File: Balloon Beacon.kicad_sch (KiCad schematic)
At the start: 51 parts, among them J1 PV Input, J2 Serial, J3 ICSP, J4 I2C, J6 GPS_ANT, Q1 AO3401A, U1 CJ431, U2 ATmega328PB-MU, U3 STC22K33048-26.000MT, U4 LM50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

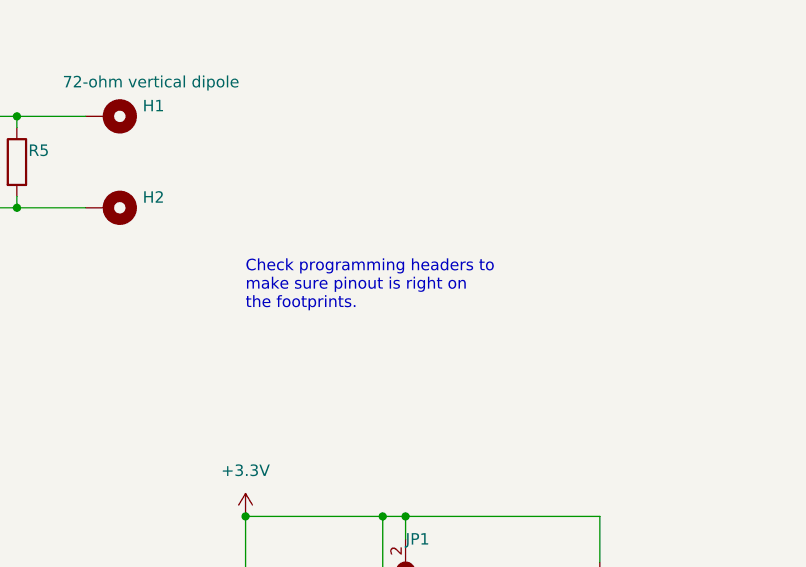
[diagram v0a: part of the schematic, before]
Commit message: Deleted note on schematic and added footprint for jumper.
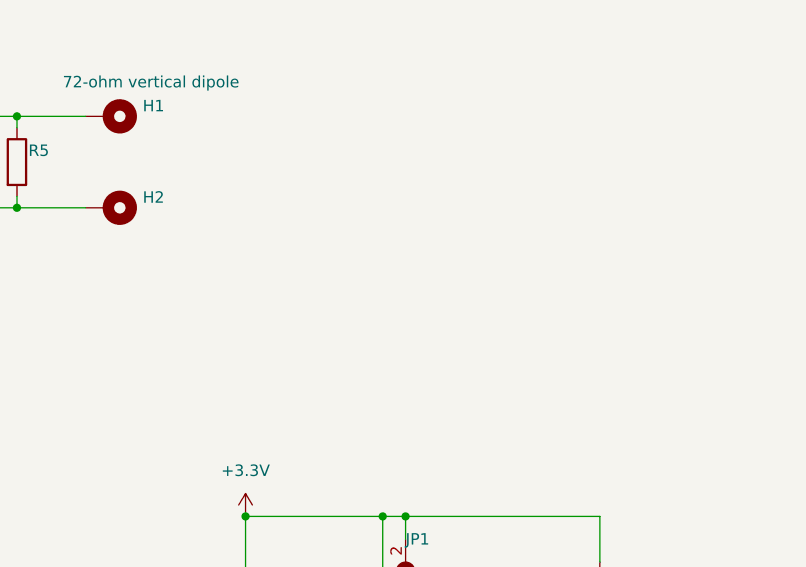
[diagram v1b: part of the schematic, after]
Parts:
- JP1: footprint (none) -> Jumper:SolderJumper-2_P1.3mm_Open_TrianglePad1.0x1.5mm
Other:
- note removed: "Check programming headers to make sure pinout is right on the footprints."
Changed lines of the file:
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@@
-    (effects (font (size 1.27 1.27)) (justify left bottom))
-  )
-  (text "Check programming headers to \nmake sure pinout is right on\nthe footprints."
-    (at 205.74 58.42 0)
     (effects (font (size 1.27 1.27)) (justify left bottom))
   )
@@
       (effects (font (size 1.27 1.27)) (justify right) hide)
     )
-    (property "Footprint" "" (id 2) (at 223.52 87.63 0)
+    (property "Footprint" "Jumper:SolderJumper-2_P1.3mm_Open_TrianglePad1.0x1.5mm" (id 2) (at 223.52 87.63 0)
       (effects (font (size 1.27 1.27)) hide)
     )
@@
     )
     (path "/7acad855-ca17-4ab1-8fa0-6bf876855ebd"
-      (reference "JP1") (unit 1) (value "SolderJumper_2_Open") (footprint "")
+      (reference "JP1") (unit 1) (value "SolderJumper_2_Open") (footprint "Jumper:SolderJumper-2_P1.3mm_Open_TrianglePad1.0x1.5mm")
     )
     (path "/38660ac3-4961-47b0-bbb6-8ac190a31e1a"

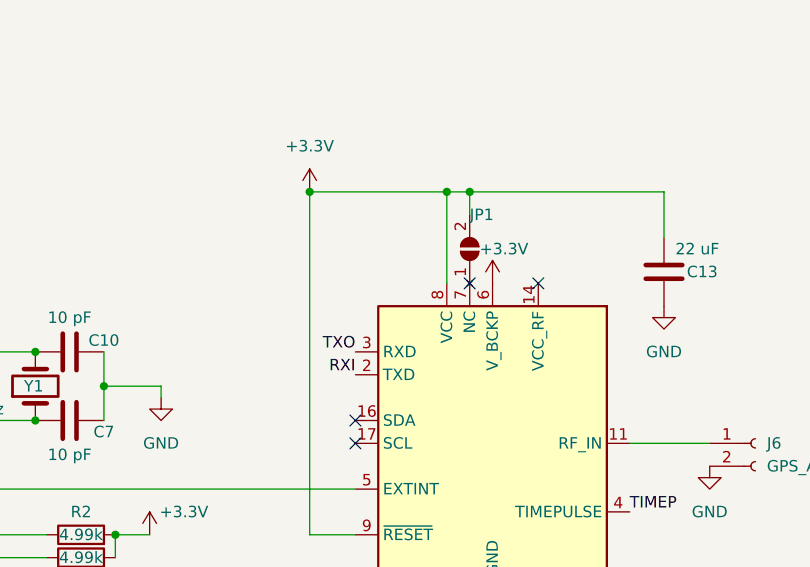
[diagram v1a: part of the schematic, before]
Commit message: Fixed no connect on GPS...
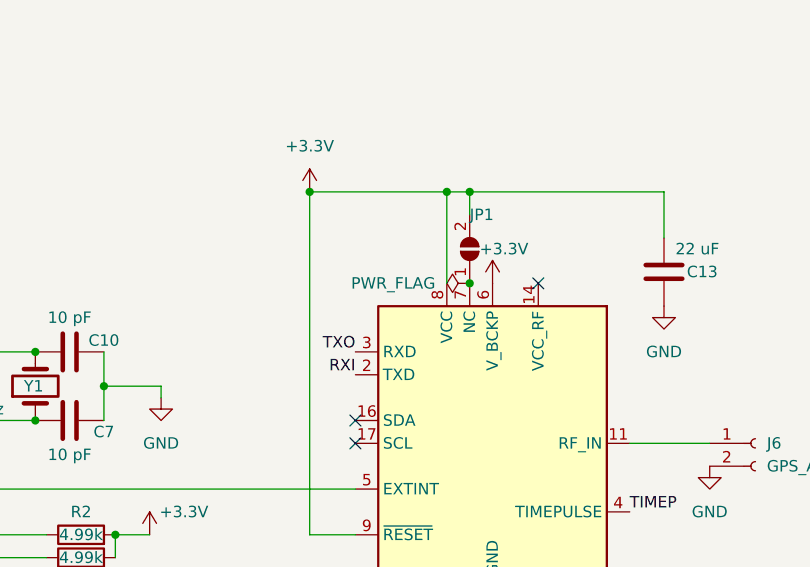
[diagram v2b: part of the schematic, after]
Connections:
- no-connect marks 15 -> 14
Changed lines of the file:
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@@
   (junction (at 205.74 81.28) (diameter 0) (color 0 0 0 0)
+  )
+  (junction (at 223.52 91.44) (diameter 0) (color 0 0 0 0)
   )
   (junction (at 182.88 102.87) (diameter 0) (color 0 0 0 0)
@@
   (no_connect (at 81.28 41.91))
   (no_connect (at 55.88 39.37))
-  (no_connect (at 223.52 91.44))
   (no_connect (at 170.18 41.91))
   (no_connect (at 20.32 34.29))
@@
     (pin "1")
   )
+  (symbol (lib_id "power:PWR_FLAG") (at 223.52 91.44 90) (unit 1)
+    (in_bom yes) (on_board yes) (fields_autoplaced)
+    (property "Reference" "#FLG?" (id 0) (at 221.615 91.44 0)
+      (effects (font (size 1.27 1.27)) hide)
+    )
+    (property "Value" "PWR_FLAG" (id 1) (at 219.71 91.4399 90)
+      (effects (font (size 1.27 1.27)) (justify left))
+    )
+    (property "Footprint" "" (id 2) (at 223.52 91.44 0)
+      (effects (font (size 1.27 1.27)) hide)
+    )
+    (property "Datasheet" "~" (id 3) (at 223.52 91.44 0)
+      (effects (font (size 1.27 1.27)) hide)
+    )
+    (pin "1")
+  )
   (symbol (lib_id "Connector:Conn_01x02_Female") (at 255.27 109.22 0) (unit 1)
     (in_bom yes) (on_board yes) (fields_autoplaced)
@@
       (reference "#FLG0104") (unit 1) (value "PWR_FLAG") (footprint "")
     )
+    (path "/e752b3c5-19d9-412d-8084-a1d633460973"
+      (reference "#FLG?") (unit 1) (value "PWR_FLAG") (footprint "")
+    )
     (path "/39681a7e-93cb-47f8-bfb9-0aecbadbf696"

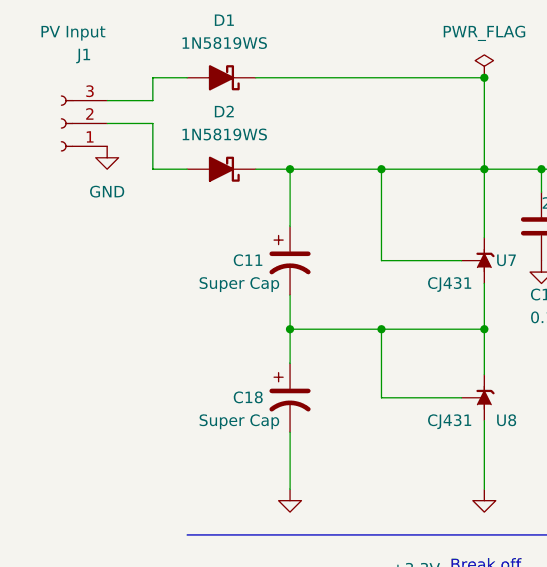
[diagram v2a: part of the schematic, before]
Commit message: Added a solar cell so you can see what might work...
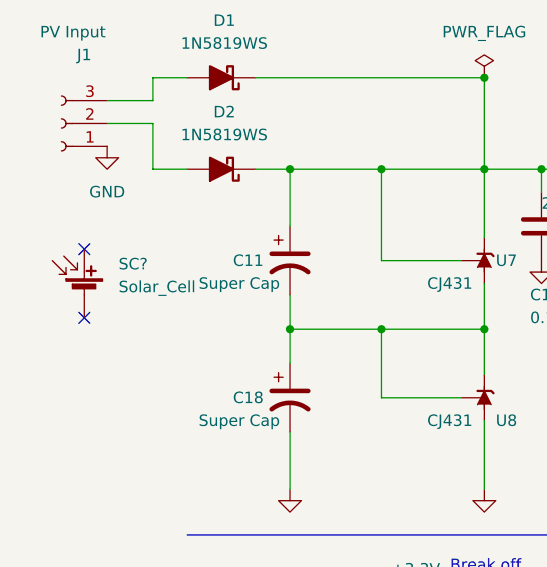
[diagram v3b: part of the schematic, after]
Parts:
- added SC?: Solar_Cell, symbol Device:Solar_Cell
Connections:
- no-connect marks 14 -> 16
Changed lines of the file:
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@@
   (no_connect (at 210.82 106.68))
   (no_connect (at 210.82 109.22))
+  (no_connect (at 20.32 118.11))
+  (no_connect (at 20.32 125.73))
   (no_connect (at 156.21 86.36))
   (no_connect (at 156.21 88.9))
@@
     (pin "1")
   )
+  (symbol (lib_id "Device:Solar_Cell") (at 20.32 123.19 0) (unit 1)
+    (in_bom yes) (on_board yes) (fields_autoplaced)
+    (property "Reference" "SC?" (id 0) (at 24.13 119.7609 0)
+      (effects (font (size 1.27 1.27)) (justify left))
+    )
+    (property "Value" "Solar_Cell" (id 1) (at 24.13 122.3009 0)
+      (effects (font (size 1.27 1.27)) (justify left))
+    )
+    (property "Footprint" "" (id 2) (at 20.32 121.666 90)
+      (effects (font (size 1.27 1.27)) hide)
+    )
+    (property "Datasheet" "https://www.mouser.com/ProductDetail/PowerFilm/MPT36-75?qs=BJlw7L4Cy79PADpX3LN7rA%3D%3D" (id 3) (at 20.32 121.666 90)
+      (effects (font (size 1.27 1.27)) hide)
+    )
+    (pin "1")
+    (pin "2")
+  )
   (symbol (lib_id "Device:C") (at 45.72 34.29 270) (unit 1)
     (in_bom yes) (on_board yes)
@@
   (symbol (lib_id "power:PWR_FLAG") (at 223.52 91.44 90) (unit 1)
     (in_bom yes) (on_board yes) (fields_autoplaced)
-    (property "Reference" "#FLG?" (id 0) (at 221.615 91.44 0)
+    (property "Reference" "#FLG0103" (id 0) (at 221.615 91.44 0)
       (effects (font (size 1.27 1.27)) hide)
     )
@@
       (reference "#FLG0102") (unit 1) (value "PWR_FLAG") (footprint "")
     )
+    (path "/e752b3c5-19d9-412d-8084-a1d633460973"
+      (reference "#FLG0103") (unit 1) (value "PWR_FLAG") (footprint "")
+    )
     (path "/578ae771-eb1e-452e-ad8f-2873091bd97f"
       (reference "#FLG0104") (unit 1) (value "PWR_FLAG") (footprint "")
     )
-    (path "/e752b3c5-19d9-412d-8084-a1d633460973"
-      (reference "#FLG?") (unit 1) (value "PWR_FLAG") (footprint "")
-    )
     (path "/39681a7e-93cb-47f8-bfb9-0aecbadbf696"
       (reference "#PWR01") (unit 1) (value "GND") (footprint "")
@@
       (reference "R8") (unit 1) (value "100") (footprint "Resistor_SMD:R_0603_1608Metric_Pad0.98x0.95mm_HandSolder")
     )
+    (path "/636dce35-ff98-43a1-aeb4-4c95a15832a9"
+      (reference "SC?") (unit 1) (value "Solar_Cell") (footprint "")
+    )
     (path "/02163717-eac1-4757-bdb2-c94f527ed6dd"

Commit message: Changed JLCPCB to LCSC for compatibility with https://support.jlcpcb.com/article/84-how-to-generate-the-bom-and-centroid-file-from-kicad
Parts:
- C10, C7: JLCPCB C1634 -> (none); LCSC (none) -> C1634
- C12, C14, C15, C16, C17, C19, C5, C6, C8, C9: JLCPCB C1525 -> (none); LCSC (none) -> C1525
- C13, C3: JLCPCB C59461 -> (none); LCSC (none) -> C59461
- C2: JLCPCB C1620 -> (none); LCSC (none) -> C1620
- C4: JLCPCB C51207 -> (none); LCSC (none) -> C51207
- D1, D2: JLCPCB C191023 -> (none); LCSC (none) -> C191023
- D4: JLCPCB C2293 -> (none); LCSC (none) -> C2293
- Q1: JLCPCB C15127 -> (none); LCSC (none) -> C15127
- R1, R5: JLCPCB C17490 -> (none); LCSC (none) -> C17490
- R2, R3: JLCPCB C23046 -> (none); LCSC (none) -> C23046
- R4: JLCPCB C22843 -> (none); LCSC (none) -> C22843
- R6: JLCPCB C23172 -> (none); LCSC (none) -> C23172
- R7: JLCPCB C25741 -> (none); LCSC (none) -> C25741
- R8: JLCPCB C22775 -> (none); LCSC (none) -> C22775
- U1, U7, U8: JLCPCB C3113 -> (none); LCSC (none) -> C3113
- U2: JLCPCB C967933 -> (none); LCSC (none) -> C967933
- U4: JLCPCB C411880 -> (none); LCSC (none) -> C411880
- U5: JLCPCB C504891 -> (none); LCSC (none) -> C504891
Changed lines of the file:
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@@
       (effects (font (size 1.27 1.27) italic) hide)
     )
-    (property "JLCPCB" "C3113" (id 4) (at 102.87 119.38 90)
+    (property "LCSC" "C3113" (id 4) (at 102.87 119.38 90)
       (effects (font (size 1.27 1.27)) hide)
     )
@@
       (effects (font (size 1.27 1.27)) hide)
     )
-    (property "JLCPCB" "C23046" (id 4) (at 180.34 119.38 90)
+    (property "LCSC" "C23046" (id 4) (at 180.34 119.38 90)
       (effects (font (size 1.27 1.27)) hide)
     )
@@
       (effects (font (size 1.27 1.27)) hide)
     )
-    (property "JLCPCB" "C1525" (id 4) (at 115.57 20.32 0)
+    (property "LCSC" "C1525" (id 4) (at 115.57 20.32 0)
       (effects (font (size 1.27 1.27)) hide)
     )
@@
       (effects (font (size 1.27 1.27)) hide)
     )
-    (property "JLCPCB" "C23046" (id 4) (at 180.34 121.92 90)
+    (property "LCSC" "C23046" (id 4) (at 180.34 121.92 90)
       (effects (font (size 1.27 1.27)) hide)
     )
@@
       (effects (font (size 1.27 1.27)) hide)
     )
-    (property "JLCPCB" "C967933" (id 4) (at 140.97 116.84 0)
+    (property "LCSC" "C967933" (id 4) (at 140.97 116.84 0)
       (effects (font (size 1.27 1.27)) hide)
     )
@@
       (effects (font (size 1.27 1.27)) hide)
     )
-    (property "JLCPCB" "C1525" (id 4) (at 76.2 123.19 0)
+    (property "LCSC" "C1525" (id 4) (at 76.2 123.19 0)
       (effects (font (size 1.27 1.27)) hide)
     )
@@
       (effects (font (size 1.27 1.27)) hide)
     )
-    (property "JLCPCB" "C1525" (id 4) (at 58.42 74.93 0)
+    (property "LCSC" "C1525" (id 4) (at 58.42 74.93 0)
       (effects (font (size 1.27 1.27)) hide)
     )
@@
       (effects (font (size 1.27 1.27)) hide)
     )
-    (property "JLCPCB" "C22843" (id 4) (at 86.36 24.13 90)
+    (property "LCSC" "C22843" (id 4) (at 86.36 24.13 90)
       (effects (font (size 1.27 1.27)) hide)
     )
@@
       (effects (font (size 1.27 1.27)) hide)
     )
-    (property "JLCPCB" "C15127" (id 4) (at 95.25 24.13 0)
+    (property "LCSC" "C15127" (id 4) (at 95.25 24.13 0)
       (effects (font (size 1.27 1.27)) hide)
     )
@@
       (effects (font (size 1.27 1.27)) (justify left bottom) hide)
     )
-    (property "JLCPCB" "C411880" (id 4) (at 44.45 71.12 0)
+    (property "LCSC" "C411880" (id 4) (at 44.45 71.12 0)
       (effects (font (size 1.27 1.27)) hide)
     )
@@
       (effects (font (size 1.27 1.27)) hide)
     )
-    (property "JLCPCB" "C1525" (id 4) (at 109.22 115.57 0)
+    (property "LCSC" "C1525" (id 4) (at 109.22 115.57 0)
       (effects (font (size 1.27 1.27)) hide)
     )
@@
       (effects (font (size 1.27 1.27)) hide)
     )
-    (property "JLCPCB" "C1525" (id 4) (at 45.72 34.29 0)
+    (property "LCSC" "C1525" (id 4) (at 45.72 34.29 0)
       (effects (font (size 1.27 1.27)) hide)
     )
@@
       (effects (font (size 1.27 1.27)) hide)
     )
-    (property "JLCPCB" "C1525" (id 4) (at 66.04 180.34 90)
+    (property "LCSC" "C1525" (id 4) (at 66.04 180.34 90)
       (effects (font (size 1.27 1.27)) hide)
     )
@@
       (effects (font (size 1.27 1.27)) hide)
     )
-    (property "JLCPCB" "C191023" (id 4) (at 35.56 99.06 0)
+    (property "LCSC" "C191023" (id 4) (at 35.56 99.06 0)
       (effects (font (size 1.27 1.27)) hide)
     )
@@
       (effects (font (size 1.27 1.27)) hide)
     )
-    (property "JLCPCB" "C1634" (id 4) (at 179.07 99.06 90)
+    (property "LCSC" "C1634" (id 4) (at 179.07 99.06 90)
       (effects (font (size 1.27 1.27)) hide)
     )
@@
       (effects (font (size 1.27 1.27)) hide)
     )
-    (property "JLCPCB" "C1620" (id 4) (at 138.43 41.91 0)
+    (property "LCSC" "C1620" (id 4) (at 138.43 41.91 0)
       (effects (font (size 1.27 1.27)) hide)
     )
@@
       (effects (font (size 1.27 1.27)) hide)
     )
-    (property "JLCPCB" "C59461" (id 4) (at 245.11 90.17 0)
+    (property "LCSC" "C59461" (id 4) (at 245.11 90.17 0)
       (effects (font (size 1.27 1.27)) hide)
     )
@@
       (effects (font (size 1.27 1.27)) hide)
     )
-    (property "JLCPCB" "C1634" (id 4) (at 179.07 106.68 90)
+    (property "LCSC" "C1634" (id 4) (at 179.07 106.68 90)
       (effects (font (size 1.27 1.27)) hide)
     )
@@
       (effects (font (size 1.27 1.27)) hide)
     )
-    (property "JLCPCB" "C1525" (id 4) (at 121.92 36.83 90)
+    (property "LCSC" "C1525" (id 4) (at 121.92 36.83 90)
       (effects (font (size 1.27 1.27)) hide)
     )
@@
       (effects (font (size 1.27 1.27)) hide)
     )
-    (property "JLCPCB" "C504891" (id 4) (at 68.58 41.91 0)
+    (property "LCSC" "C504891" (id 4) (at 68.58 41.91 0)
       (effects (font (size 1.27 1.27)) hide)
     )
@@
       (effects (font (size 1.27 1.27)) hide)
     )
-    (property "JLCPCB" "C23172" (id 4) (at 91.44 114.3 0)
+    (property "LCSC" "C23172" (id 4) (at 91.44 114.3 0)
       (effects (font (size 1.27 1.27)) hide)
     )
@@
       (effects (font (size 1.27 1.27)) hide)
     )
-    (property "JLCPCB" "C1525" (id 4) (at 26.67 72.39 0)
+    (property "LCSC" "C1525" (id 4) (at 26.67 72.39 0)
       (effects (font (size 1.27 1.27)) hide)
     )
@@
       (effects (font (size 1.27 1.27)) hide)
     )
-    (property "JLCPCB" "C2293" (id 4) (at 99.06 137.16 0)
+    (property "LCSC" "C2293" (id 4) (at 99.06 137.16 0)
       (effects (font (size 1.27 1.27)) hide)
     )
@@
       (effects (font (size 1.27 1.27)) hide)
     )
-    (property "JLCPCB" "C191023" (id 4) (at 35.56 109.22 0)
+    (property "LCSC" "C191023" (id 4) (at 35.56 109.22 0)
       (effects (font (size 1.27 1.27)) hide)
     )
@@
       (effects (font (size 1.27 1.27) italic) hide)
     )
-    (property "JLCPCB" "C3113" (id 4) (at 64.77 119.38 90)
+    (property "LCSC" "C3113" (id 4) (at 64.77 119.38 90)
       (effects (font (size 1.27 1.27)) hide)
     )
@@
       (effects (font (size 1.27 1.27)) hide)
     )
-    (property "JLCPCB" "C17490" (id 4) (at 180.34 41.91 0)
+    (property "LCSC" "C17490" (id 4) (at 180.34 41.91 0)
       (effects (font (size 1.27 1.27)) hide)
     )
@@
       (effects (font (size 1.27 1.27)) hide)
     )
-    (property "JLCPCB" "C25741" (id 4) (at 91.44 123.19 0)
+    (property "LCSC" "C25741" (id 4) (at 91.44 123.19 0)
       (effects (font (size 1.27 1.27)) hide)
     )
@@
       (effects (font (size 1.27 1.27)) hide)
     )
-    (property "JLCPCB" "C17490" (id 4) (at 80.01 175.26 0)
+    (property "LCSC" "C17490" (id 4) (at 80.01 175.26 0)
       (effects (font (size 1.27 1.27)) hide)
     )
@@
       (effects (font (size 1.27 1.27)) hide)
     )
-    (property "JLCPCB" "C1525" (id 4) (at 121.92 90.17 0)
+    (property "LCSC" "C1525" (id 4) (at 121.92 90.17 0)
       (effects (font (size 1.27 1.27)) hide)
     )
@@
       (effects (font (size 1.27 1.27) italic) hide)
     )
-    (property "JLCPCB" "C3113" (id 4) (at 64.77 134.62 90)
+    (property "LCSC" "C3113" (id 4) (at 64.77 134.62 90)
       (effects (font (size 1.27 1.27)) hide)
     )
@@
       (effects (font (size 1.27 1.27)) hide)
     )
-    (property "JLCPCB" "C1525" (id 4) (at 148.59 69.4377 0)
+    (property "LCSC" "C1525" (id 4) (at 148.59 69.4377 0)
       (effects (font (size 1.27 1.27)) hide)
     )
@@
       (effects (font (size 1.27 1.27)) hide)
     )
-    (property "JLCPCB" "C59461" (id 4) (at 71.12 115.57 0)
+    (property "LCSC" "C59461" (id 4) (at 71.12 115.57 0)
       (effects (font (size 1.27 1.27)) hide)
     )
@@
       (effects (font (size 1.27 1.27)) hide)
     )
-    (property "JLCPCB" "C51207" (id 4) (at 148.59 41.91 0)
+    (property "LCSC" "C51207" (id 4) (at 148.59 41.91 0)
       (effects (font (size 1.27 1.27)) hide)
     )
@@
       (effects (font (size 1.27 1.27)) hide)
     )
-    (property "JLCPCB" "C22775" (id 4) (at 91.44 137.16 90)
-      (effects (font (size 1.27 1.27)) hide)
-    )
+    (property "LCSC" "C22775" (id 4) (at 91.44 137.16 90)
+      (effects (font (size 1.27 1.27)) hide)
+    )
